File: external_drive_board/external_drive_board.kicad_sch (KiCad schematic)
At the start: 7 parts, among them J1 MD-90SM, J2 MD-90SM, SW1 SW_DIP_x04

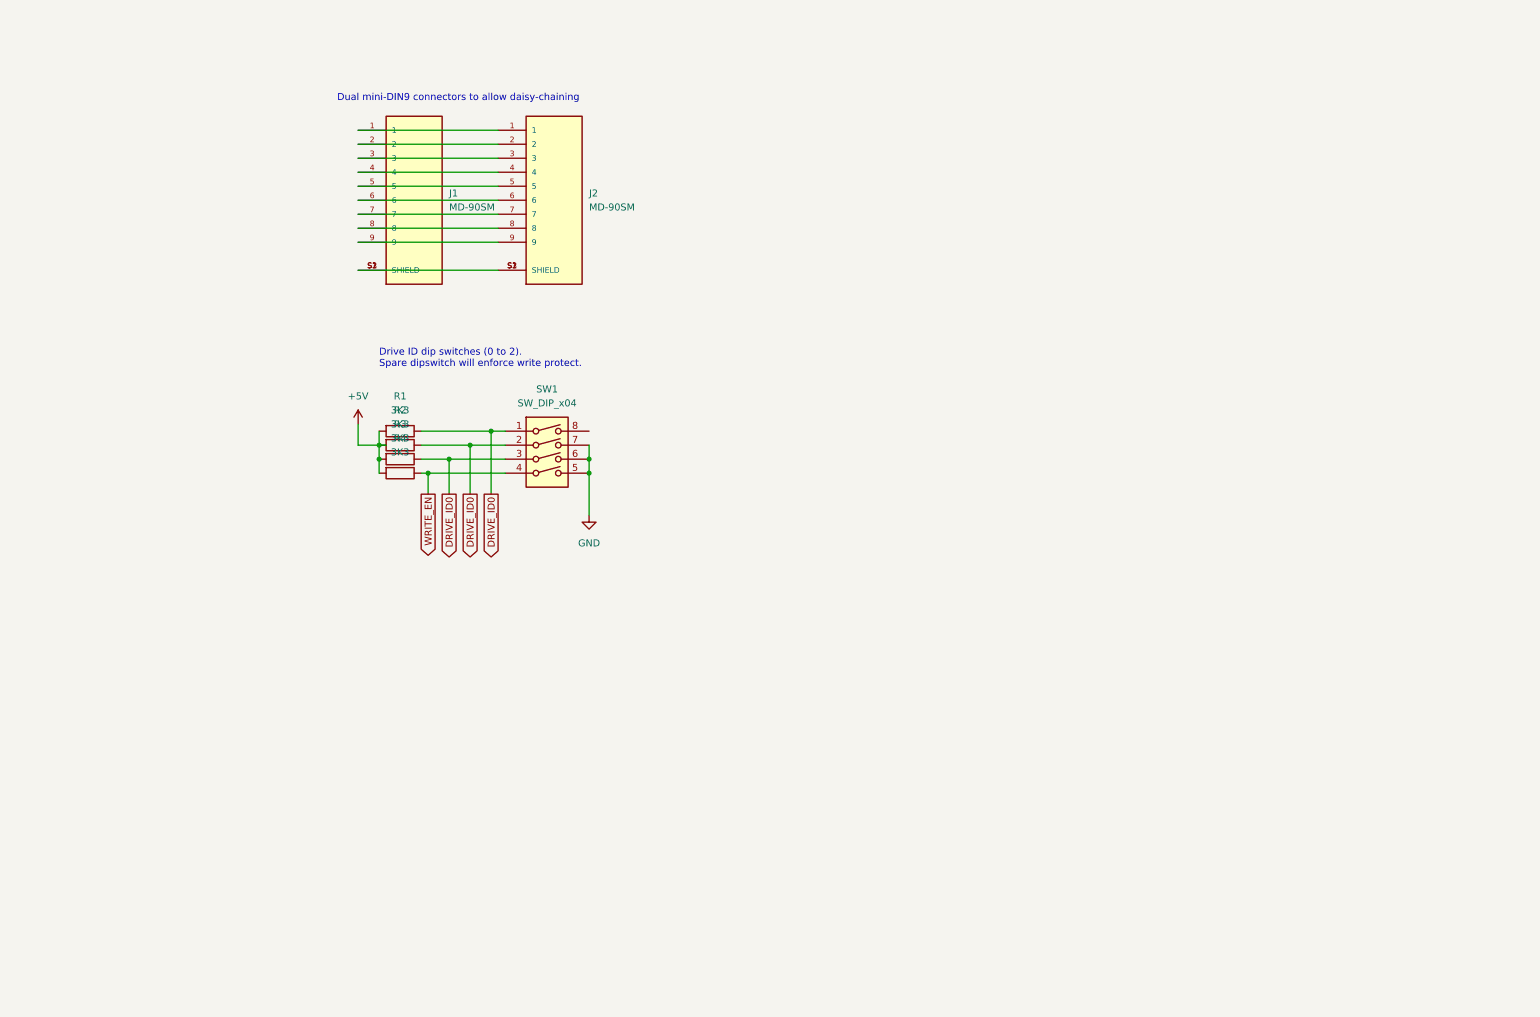
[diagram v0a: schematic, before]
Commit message: add more logic to C1565 board
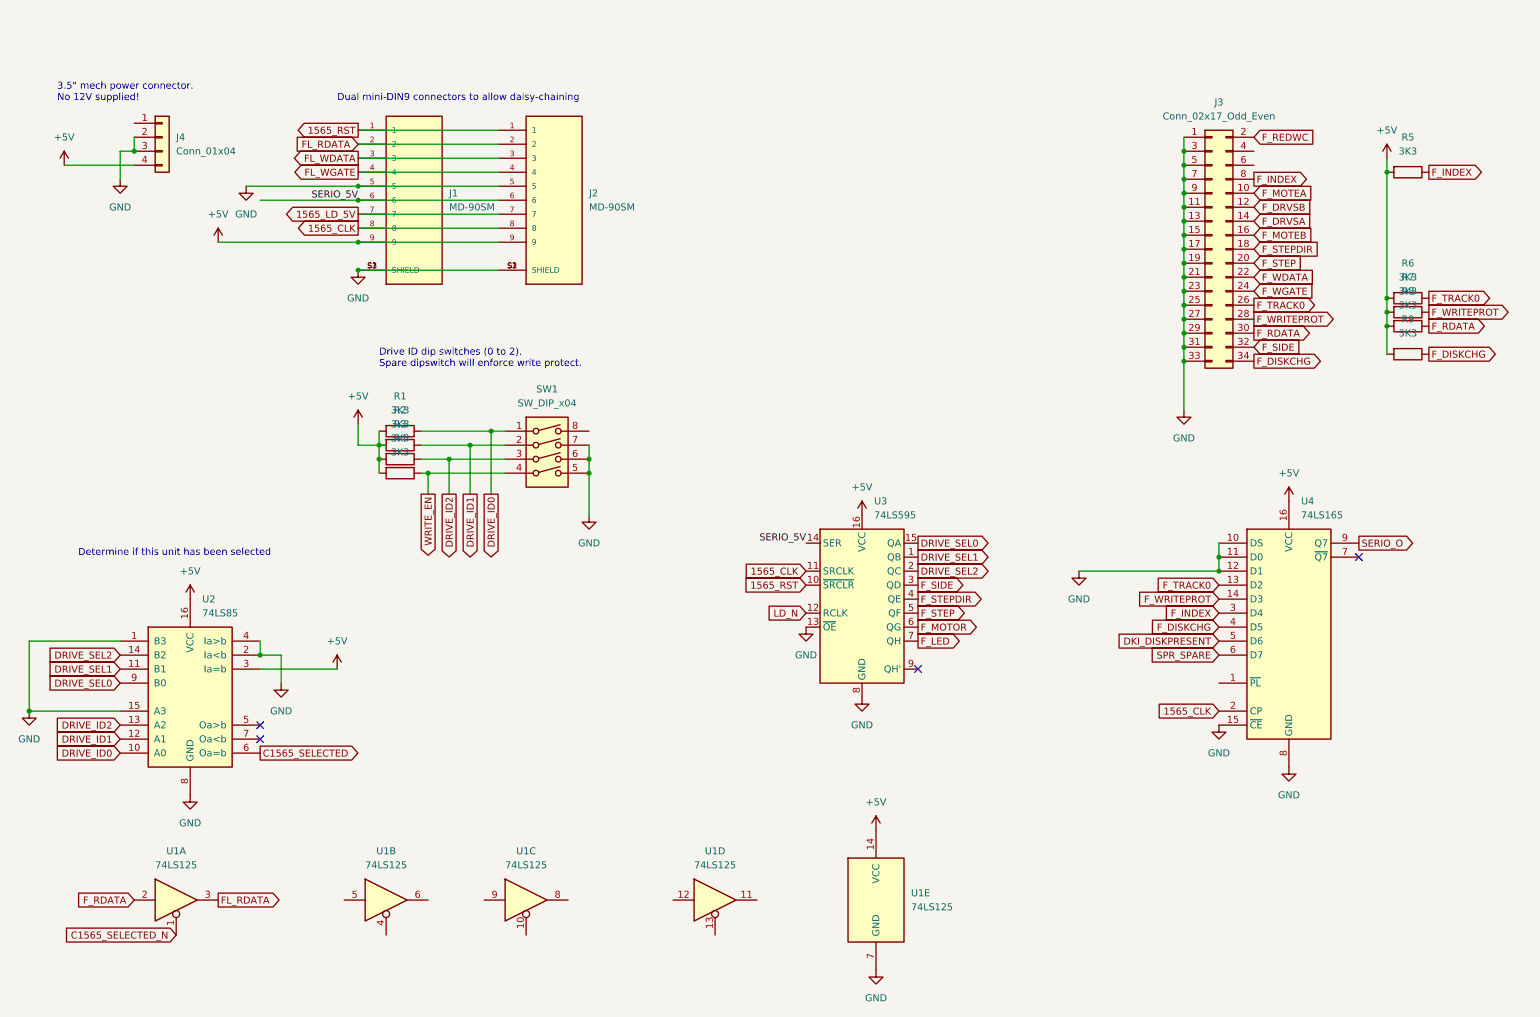
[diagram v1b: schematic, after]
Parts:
- added J3: Conn_02x17_Odd_Even, Connector_PinHeader_2.54mm:PinHeader_2x17_P2.54mm_Vertical, symbol Connector_Generic:Conn_02x17_Odd_Even
- added J4: Conn_01x04, Connector_PinHeader_2.54mm:PinHeader_1x04_P2.54mm_Vertical, symbol Connector_Generic:Conn_01x04
- added R5, R6, R7, R8, R9: 3K3, Resistor_THT:R_Axial_DIN0207_L6.3mm_D2.5mm_P7.62mm_Horizontal, symbol Device:R
- added U1: 74LS125, symbol 74xx:74LS125
- added U2: 74LS85, symbol 74xx:74LS85
- added U3: 74LS595, symbol 74xx:74LS595
- added U4: 74LS165, symbol 74xx:74LS165
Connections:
- net +5V: now also J1.9, J2.9, J4.4 (Pin_4), R5.2, R6.2, R7.2, R8.2, R9.2, U1.14 (VCC), U2.16 (VCC), U2.3 (Ia=b), U3.16 (VCC), U4.16 (VCC)
- net DRIVE_ID0: now also U2.10 (A0); no longer R2.1, R3.1, SW1.2, SW1.3
- net GND: now also J1.5, J1.S1 (SHIELD), J1.S2 (SHIELD), J1.S3 (SHIELD), J2.5, J2.S1 (SHIELD), J2.S2 (SHIELD), J2.S3 (SHIELD), J3.1 (Pin_1), J3.11 (Pin_11), J3.13 (Pin_13), J3.15 (Pin_15), J3.17 (Pin_17), J3.19 (Pin_19), J3.21 (Pin_21), J3.23 (Pin_23), J3.25 (Pin_25), J3.27 (Pin_27), J3.29 (Pin_29), J3.3 (Pin_3), J3.31 (Pin_31), J3.33 (Pin_33), J3.5 (Pin_5), J3.7 (Pin_7), J3.9 (Pin_9), J4.2 (Pin_2), J4.3 (Pin_3), U1.7 (GND), U2.1 (B3), U2.15 (A3), U2.2 (Ia<b), U2.4 (Ia>b), U2.8 (GND), U3.13 (~{OE}), U3.8 (GND), U4.10 (DS), U4.11 (D0), U4.12 (D1), U4.15 (~{CE}), U4.8 (GND)
- net 1565_RST: now reaches J1.1, J2.1
- net 1565_RST: now also U3.10 (~{SRCLR})
- net FL_RDATA: now reaches J1.2, J2.2
- net FL_RDATA: now also U1.3
- net FL_WDATA: now reaches J1.3, J2.3
- net FL_WGATE: now reaches J1.4, J2.4
- net SERIO_5V: now reaches J1.6, J2.6
- net SERIO_5V: now also U3.14 (SER)
- net 1565_LD_5V: now reaches J1.7, J2.7
- net 1565_CLK: now reaches J1.8, J2.8
- net 1565_CLK: now also U3.11 (SRCLK), U4.2 (CP)
- new net C1565_SELECTED: U2.6 (Oa=b)
- new net C1565_SELECTED_N: U1.1
- new net DKI_DISKPRESENT: U4.5 (D6)
- new net DRIVE_ID1: R2.1, SW1.2, U2.12 (A1)
- new net DRIVE_ID2: R3.1, SW1.3, U2.13 (A2)
- new net DRIVE_SEL0: U2.9 (B0), U3.15 (QA)
- new net DRIVE_SEL1: U2.11 (B1), U3.1 (QB)
- new net DRIVE_SEL2: U2.14 (B2), U3.2 (QC)
- new net F_DISKCHG: J3.34 (Pin_34), R9.1, U4.4 (D5)
- new net F_DRVSA: J3.14 (Pin_14)
- new net F_DRVSB: J3.12 (Pin_12)
- new net F_INDEX: J3.8 (Pin_8), R5.1, U4.3 (D4)
- new net F_LED: U3.7 (QH)
- new net F_MOTEA: J3.10 (Pin_10)
- new net F_MOTEB: J3.16 (Pin_16)
- new net F_MOTOR: U3.6 (QG)
- new net F_RDATA: J3.30 (Pin_30), R8.1, U1.2
- new net F_REDWC: J3.2 (Pin_2)
- new net F_SIDE: J3.32 (Pin_32), U3.3 (QD)
- new net F_STEP: J3.20 (Pin_20), U3.5 (QF)
- new net F_STEPDIR: J3.18 (Pin_18), U3.4 (QE)
- new net F_TRACK0: J3.26 (Pin_26), R6.1, U4.13 (D2)
- new net F_WDATA: J3.22 (Pin_22)
- new net F_WGATE: J3.24 (Pin_24)
- new net F_WRITEPROT: J3.28 (Pin_28), R7.1, U4.14 (D3)
- new net LD_N: U3.12 (RCLK)
- new net SERIO_O: U4.9 (Q7)
- new net SPR_SPARE: U4.6 (D7)
- no-connect marks 0 -> 4
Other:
- note added: "3.5" mech power connector. No 12V supplied!"
- note added: "Determine if this unit has been selected"

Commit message: add inverter and complete schematic
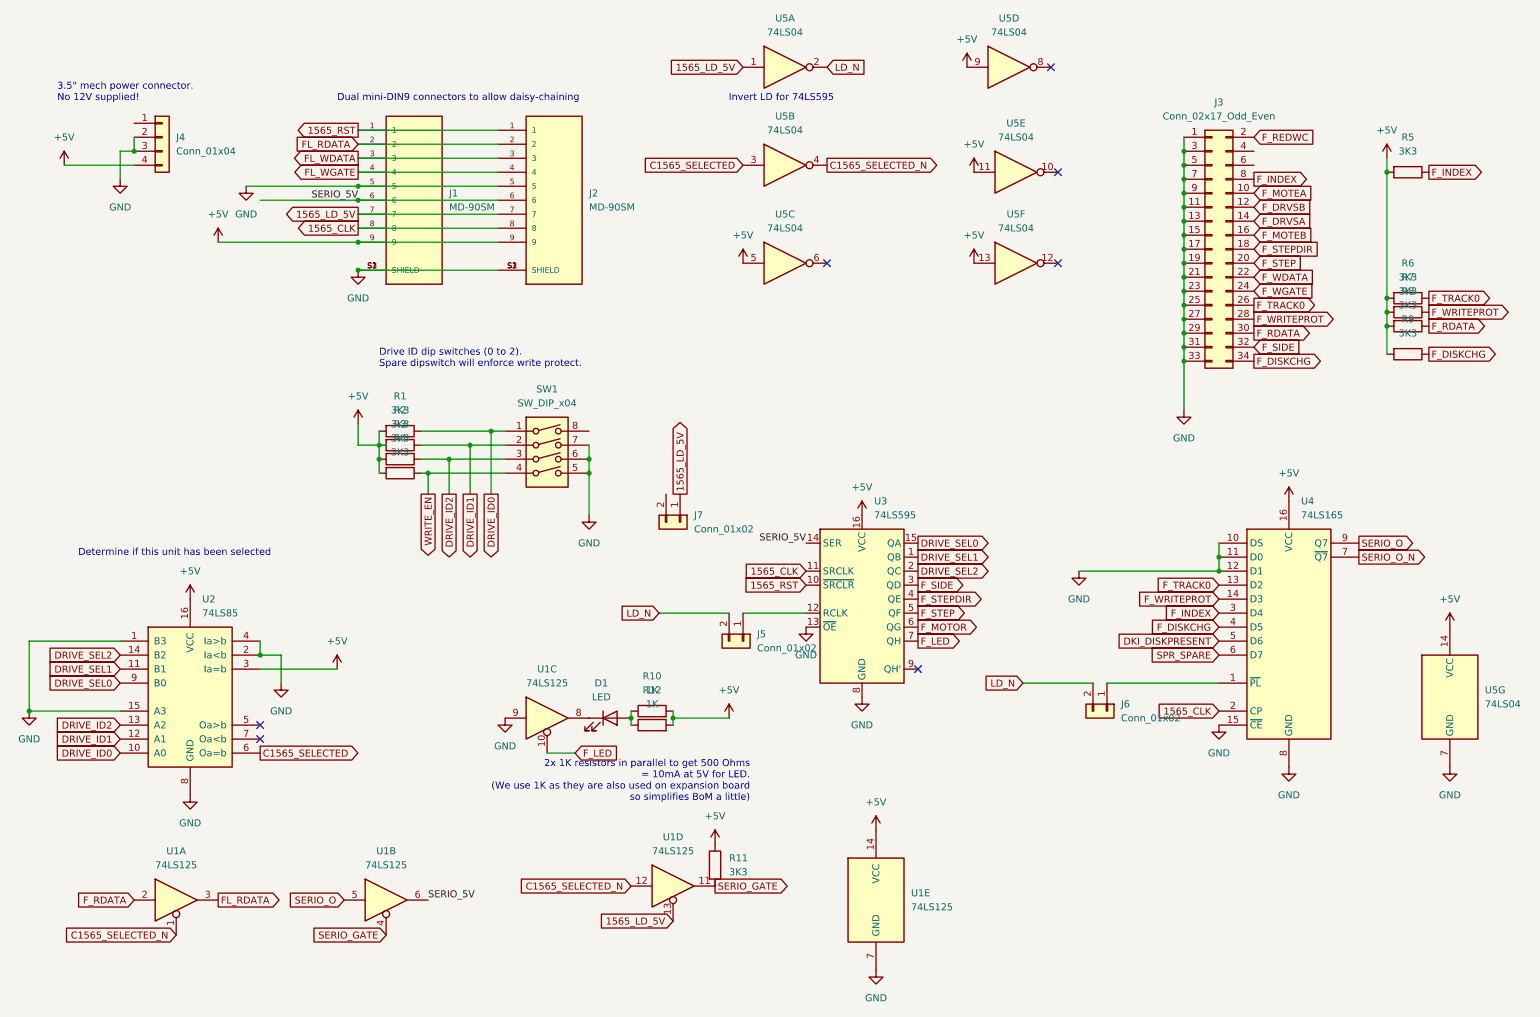
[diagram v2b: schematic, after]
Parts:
- added D1: LED, symbol Device:LED
- added J5, J6, J7: Conn_01x02, Connector_PinHeader_2.54mm:PinHeader_1x02_P2.54mm_Vertical, symbol Connector_Generic:Conn_01x02
- added R10, R12: 1K, Resistor_THT:R_Axial_DIN0207_L6.3mm_D2.5mm_P7.62mm_Horizontal, symbol Device:R
- added R11: 3K3, Resistor_THT:R_Axial_DIN0207_L6.3mm_D2.5mm_P7.62mm_Horizontal, symbol Device:R
- added U5: 74LS04, symbol 74xx:74LS04
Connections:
- net +5V: now also R10.2, R11.1, R12.2, U5.11, U5.13, U5.14 (VCC), U5.5, U5.9
- net 1565_LD_5V: now also U1.13, J7.1 (Pin_1), U5.1
- net C1565_SELECTED: now also U5.3
- net C1565_SELECTED_N: now also U1.12, U5.4
- net F_LED: now also U1.10
- net GND: now also U1.9, U5.7 (GND)
- net LD_N: now also J5.2 (Pin_2), J6.2 (Pin_2), U5.2; no longer U3.12 (RCLK)
- net SERIO_5V: now also U1.6
- net SERIO_O: now also U1.5
- net at U1.8: now also D1.1 (K)
- net at U4.1 (~{PL}): now also J6.1 (Pin_1)
- net SERIO_O_N: now reaches U4.7 (~{Q7})
- net SERIO_GATE: now reaches U1.11
- net SERIO_GATE: now also U1.4, R11.2
- new net: D1.2 (A), R10.1, R12.1
- new net: J5.1 (Pin_1), U3.12 (RCLK)
- no-connect marks 4 -> 7
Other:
- note added: "2x 1K resistors in parallel to get 500 Ohms = 10mA at 5V for LED. (We use 1K as they are also used on expansion board so simplifies BoM a little)"
- note added: "Invert LD for 74LS595"
- moved on the sheet: U1C, U1D

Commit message: begin work on layout
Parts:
- D1: footprint (none) -> LED_THT:LED_D5.0mm
- J1, J2: footprint MD-90SM:CUI_MD-90SM -> 00Project:CUI_MD-90SM
- SW1: footprint (none) -> Package_DIP:DIP-8_W7.62mm
- U1, U5: footprint (none) -> Package_DIP:DIP-14_W7.62mm
- U2, U3, U4: footprint (none) -> Package_DIP:DIP-16_W7.62mm
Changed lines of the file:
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@@
       (effects (font (size 1.27 1.27)))
     )
-    (property "Footprint" "" (at 107.95 144.78 0)
+    (property "Footprint" "Package_DIP:DIP-14_W7.62mm" (at 107.95 144.78 0)
       (effects (font (size 1.27 1.27)) hide)
     )
@@
       (effects (font (size 1.27 1.27)) (justify left))
     )
-    (property "Footprint" "" (at 242.57 128.27 0)
+    (property "Footprint" "Package_DIP:DIP-16_W7.62mm" (at 242.57 128.27 0)
       (effects (font (size 1.27 1.27)) hide)
     )
@@
       (effects (font (size 1.27 1.27)) (justify left))
     )
-    (property "Footprint" "MD-90SM:CUI_MD-90SM" (at 109.22 50.8 0)
+    (property "Footprint" "00Project:CUI_MD-90SM" (at 109.22 50.8 0)
       (effects (font (size 1.27 1.27)) (justify bottom) hide)
     )
@@
       (effects (font (size 1.27 1.27)))
     )
-    (property "Footprint" "" (at 40.64 177.8 0)
+    (property "Footprint" "Package_DIP:DIP-14_W7.62mm" (at 40.64 177.8 0)
       (effects (font (size 1.27 1.27)) hide)
     )
@@
       (effects (font (size 1.27 1.27)))
     )
-    (property "Footprint" "" (at 151.13 62.23 0)
+    (property "Footprint" "Package_DIP:DIP-14_W7.62mm" (at 151.13 62.23 0)
       (effects (font (size 1.27 1.27)) hide)
     )
@@
       (effects (font (size 1.27 1.27)))
     )
-    (property "Footprint" "" (at 151.13 26.67 0)
+    (property "Footprint" "Package_DIP:DIP-14_W7.62mm" (at 151.13 26.67 0)
       (effects (font (size 1.27 1.27)) hide)
     )
@@
       (effects (font (size 1.27 1.27)))
     )
-    (property "Footprint" "" (at 193.04 62.23 0)
+    (property "Footprint" "Package_DIP:DIP-14_W7.62mm" (at 193.04 62.23 0)
       (effects (font (size 1.27 1.27)) hide)
     )
@@
       (effects (font (size 1.27 1.27)))
     )
-    (property "Footprint" "" (at 107.95 97.79 0)
+    (property "Footprint" "Package_DIP:DIP-8_W7.62mm" (at 107.95 97.79 0)
       (effects (font (size 1.27 1.27)) hide)
     )
@@
       (effects (font (size 1.27 1.27)))
     )
-    (property "Footprint" "" (at 130.81 175.26 0)
+    (property "Footprint" "Package_DIP:DIP-14_W7.62mm" (at 130.81 175.26 0)
       (effects (font (size 1.27 1.27)) hide)
     )
@@
       (effects (font (size 1.27 1.27)) (justify left))
     )
-    (property "Footprint" "" (at 271.78 140.97 0)
+    (property "Footprint" "Package_DIP:DIP-14_W7.62mm" (at 271.78 140.97 0)
       (effects (font (size 1.27 1.27)) hide)
     )
@@
       (effects (font (size 1.27 1.27)) (justify left))
     )
-    (property "Footprint" "" (at 167.64 177.8 0)
+    (property "Footprint" "Package_DIP:DIP-14_W7.62mm" (at 167.64 177.8 0)
       (effects (font (size 1.27 1.27)) hide)
     )
@@
       (effects (font (size 1.27 1.27)))
     )
-    (property "Footprint" "" (at 151.13 44.45 0)
+    (property "Footprint" "Package_DIP:DIP-14_W7.62mm" (at 151.13 44.45 0)
       (effects (font (size 1.27 1.27)) hide)
     )
@@
       (effects (font (size 1.27 1.27)))
     )
-    (property "Footprint" "" (at 193.04 45.72 0)
+    (property "Footprint" "Package_DIP:DIP-14_W7.62mm" (at 193.04 45.72 0)
       (effects (font (size 1.27 1.27)) hide)
     )
@@
       (effects (font (size 1.27 1.27)) (justify left))
     )
-    (property "Footprint" "" (at 165.1 123.19 0)
+    (property "Footprint" "Package_DIP:DIP-16_W7.62mm" (at 165.1 123.19 0)
       (effects (font (size 1.27 1.27)) hide)
     )
@@
       (effects (font (size 1.27 1.27)))
     )
-    (property "Footprint" "" (at 78.74 177.8 0)
+    (property "Footprint" "Package_DIP:DIP-14_W7.62mm" (at 78.74 177.8 0)
       (effects (font (size 1.27 1.27)) hide)
     )
@@
       (effects (font (size 1.27 1.27)) (justify left))
     )
-    (property "Footprint" "MD-90SM:CUI_MD-90SM" (at 83.82 50.8 0)
+    (property "Footprint" "00Project:CUI_MD-90SM" (at 83.82 50.8 0)
       (effects (font (size 1.27 1.27)) (justify bottom) hide)
     )
@@
       (effects (font (size 1.27 1.27)))
     )
-    (property "Footprint" "" (at 191.77 26.67 0)
+    (property "Footprint" "Package_DIP:DIP-14_W7.62mm" (at 191.77 26.67 0)
       (effects (font (size 1.27 1.27)) hide)
     )
@@
       (effects (font (size 1.27 1.27)) (justify left))
     )
-    (property "Footprint" "" (at 43.18 140.97 0)
+    (property "Footprint" "Package_DIP:DIP-16_W7.62mm" (at 43.18 140.97 0)
       (effects (font (size 1.27 1.27)) hide)
     )
@@
       (effects (font (size 1.27 1.27)))
     )
-    (property "Footprint" "" (at 119.38 144.78 0)
-      (effects (font (size 1.27 1.27)) hide)
-    )
+    (property "Footprint" "LED_THT:LED_D5.0mm" (at 119.38 144.78 0)
+      (effects (font (size 1.27 1.27)) hide)
+    )
